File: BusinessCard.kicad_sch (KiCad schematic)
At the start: 4 parts, among them U1 NT3H2111W0FHKH

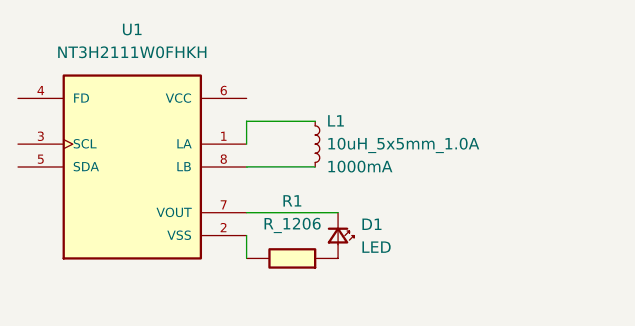
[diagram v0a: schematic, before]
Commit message: logos added to footprint
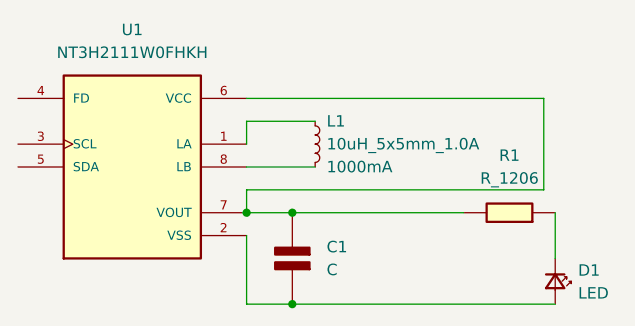
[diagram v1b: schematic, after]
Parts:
- added C1: C, PCM_4ms_Capacitor:CP_Elec_5x5.3, symbol PCM_Elektuur:C
- L1: footprint PCM_SparkFun-Coil:Inductor_4.7x4.7mm -> nfc:25X48MM_NFC_ANTENNA
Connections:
- net at U1.2 (VSS): now also D1.2 (A), C1.1 (+); no longer R1.1
- net at U1.6 (VCC): now also R1.1, U1.7 (VOUT), C1.2 (-)
- net at D1.1 (K): now also R1.2; no longer U1.7 (VOUT)
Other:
- moved on the sheet: D1, R1
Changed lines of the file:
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@@
 	(generator_version "9.0")
 	(paper "A4")
-	(wire
-		(pts
-			(xy 142.24 113.03) (xy 152.4 113.03)
+	(junction
+		(at 147.32 123.19)
+		(diameter 0)
+		(color 0 0 0 0)
+	)
+	(junction
+		(at 147.32 113.03)
+		(diameter 0)
+		(color 0 0 0 0)
+	)
+	(junction
+		(at 142.24 113.03)
+		(diameter 0)
+		(color 0 0 0 0)
+	)
+	(wire
+		(pts
+			(xy 147.32 123.19) (xy 142.24 123.19)
+		)
+		(stroke
+			(width 0)
+			(type default)
+		)
+	)
+	(wire
+		(pts
+			(xy 142.24 115.57) (xy 142.24 123.19)
+		)
+		(stroke
+			(width 0)
+			(type default)
+		)
+	)
+	(wire
+		(pts
+			(xy 142.24 100.33) (xy 175.26 100.33)
+		)
+		(stroke
+			(width 0)
+			(type default)
+		)
+	)
+	(wire
+		(pts
+			(xy 147.32 113.03) (xy 142.24 113.03)
+		)
+		(stroke
+			(width 0)
+			(type default)
+		)
+	)
+	(wire
+		(pts
+			(xy 175.26 100.33) (xy 175.26 110.49)
+		)
+		(stroke
+			(width 0)
+			(type default)
+		)
+	)
+	(wire
+		(pts
+			(xy 166.37 113.03) (xy 147.32 113.03)
+		)
+		(stroke
+			(width 0)
+			(type default)
+		)
+	)
+	(wire
+		(pts
+			(xy 176.53 118.11) (xy 176.53 113.03)
 		)
 		(stroke
@@
 	(wire
 		(pts
-			(xy 142.24 118.11) (xy 142.24 115.57)
+			(xy 142.24 110.49) (xy 142.24 113.03)
+		)
+		(stroke
+			(width 0)
+			(type default)
+		)
+	)
+	(wire
+		(pts
+			(xy 175.26 110.49) (xy 142.24 110.49)
 		)
 		(stroke
@@
 		(pts
 			(xy 149.86 102.87) (xy 142.24 102.87)
+		)
+		(stroke
+			(width 0)
+			(type default)
+		)
+	)
+	(wire
+		(pts
+			(xy 147.32 123.19) (xy 176.53 123.19)
 		)
 		(stroke
@@
 			)
 		)
-		(property "Footprint" "PCM_SparkFun-Coil:Inductor_4.7x4.7mm"
+		(property "Footprint" "nfc:25X48MM_NFC_ANTENNA"
 			(at 142.24 105.41 0)
 			(effects
@@
 				(path "/3ea08817-d3b1-4822-a9a3-fd820d6f9c9b"
 					(reference "L1")
+					(unit 1)
+				)
+			)
+		)
+	)
+	(symbol
+		(lib_id "PCM_Elektuur:C")
+		(at 147.32 118.11 180)
+		(unit 1)
+		(exclude_from_sim no)
+		(in_bom yes)
+		(on_board yes)
+		(dnp no)
+		(fields_autoplaced yes)
+		(property "Reference" "C1"
+			(at 151.13 116.8399 0)
+			(effects
+				(font
+					(size 1.27 1.27)
+				)
+				(justify right)
+			)
+		)
+		(property "Value" "C"
+			(at 151.13 119.3799 0)
+			(effects
+				(font
+					(size 1.27 1.27)
+				)
+				(justify right)
+			)
+		)
+		(property "Footprint" "PCM_4ms_Capacitor:CP_Elec_5x5.3"
+			(at 147.32 118.11 0)
+			(effects
+				(font
+					(size 1.27 1.27)
+				)
+				(hide yes)
+			)
+		)
+		(property "Datasheet" ""
+			(at 147.32 118.11 0)
+			(effects
+				(font
+					(size 1.27 1.27)
+				)
+				(hide yes)
+			)
+		)
+		(property "Description" "capacitor, non-polarized/bipolar"
+			(at 147.32 118.11 0)
+			(effects
+				(font
+					(size 1.27 1.27)
+				)
+				(hide yes)
+			)
+		)
+		(property "Indicator" "+"
+			(at 148.59 121.285 0)
+			(effects
+				(font
+					(size 1.27 1.27)
+				)
+				(hide yes)
+			)
+		)
+		(property "Rating" "V"
+			(at 147.955 114.935 0)
+			(effects
+				(font
+					(size 1.27 1.27)
+				)
+				(justify right)
+				(hide yes)
+			)
+		)
+		(pin "1"
+		)
+		(pin "2"
+		)
+		(instances
+			(project ""
+				(path "/3ea08817-d3b1-4822-a9a3-fd820d6f9c9b"
+					(reference "C1")
 					(unit 1)
 				)
@@
 	(symbol
 		(lib_id "PCM_fab:R_1206")
-		(at 147.32 118.11 90)
+		(at 171.45 113.03 90)
 		(unit 1)
 		(exclude_from_sim no)
@@
 		(fields_autoplaced yes)
 		(property "Reference" "R1"
-			(at 147.32 111.76 90)
+			(at 171.45 106.68 90)
 			(effects
 				(font
@@
 		)
 		(property "Value" "R_1206"
-			(at 147.32 114.3 90)
+			(at 171.45 109.22 90)
 			(effects
 				(font
@@
 		)
 		(property "Footprint" "PCM_fab:R_1206"
-			(at 147.32 118.11 90)
+			(at 171.45 113.03 90)
 			(effects
 				(font
@@
 		)
 		(property "Datasheet" "~"
-			(at 147.32 118.11 0)
+			(at 171.45 113.03 0)
 			(effects
 				(font
@@
 		)
 		(property "Description" "Resistor"
-			(at 147.32 118.11 0)
+			(at 171.45 113.03 0)
 			(effects
 				(font
@@
 	(symbol
 		(lib_id "PCM_SparkFun-LED:LED")
-		(at 152.4 115.57 270)
+		(at 176.53 120.65 270)
 		(unit 1)
 		(exclude_from_sim no)
@@
 		(fields_autoplaced yes)
 		(property "Reference" "D1"
-			(at 154.94 114.3634 90)
+			(at 179.07 119.4434 90)
 			(effects
 				(font
@@
 		)
 		(property "Value" "LED"
-			(at 154.94 116.9034 90)
+			(at 179.07 121.9834 90)
 			(effects
 				(font
@@
 		)
 		(property "Footprint" "PCM_SparkFun-LED:LED_0603_1608Metric"
-			(at 147.32 115.57 0)
+			(at 171.45 120.65 0)
 			(effects
 				(font
@@
 		)
 		(property "Datasheet" "~"
-			(at 144.78 115.57 0)
+			(at 168.91 120.65 0)
 			(effects
 				(font
@@
 		)
 		(property "Description" "Light emitting diode"
-			(at 139.7 115.57 0)
+			(at 163.83 120.65 0)
 			(effects
 				(font
@@
 		)
 		(property "PROD_ID" "LED-"
-			(at 142.24 115.57 0)
-			(effects
-				(font
+			(at 166.37 120.65 0)
+			(effects
+				(font

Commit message: Made a few design changes, started the intro
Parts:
- C1: footprint PCM_4ms_Capacitor:CP_Elec_5x5.3 -> nfc:CAPC1608X90N
- D1: footprint PCM_SparkFun-LED:LED_0603_1608Metric -> nfc:LED0805-R-RD
- R1: footprint PCM_fab:R_1206 -> nfc:C0603
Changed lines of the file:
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@@
 			)
 		)
-		(property "Footprint" "PCM_4ms_Capacitor:CP_Elec_5x5.3"
+		(property "Footprint" "nfc:CAPC1608X90N"
 			(at 147.32 118.11 0)
 			(effects
@@
 			)
 		)
-		(property "Footprint" "PCM_fab:R_1206"
+		(property "Footprint" "nfc:C0603"
 			(at 171.45 113.03 90)
 			(effects
@@
 			)
 		)
-		(property "Footprint" "PCM_SparkFun-LED:LED_0603_1608Metric"
+		(property "Footprint" "nfc:LED0805-R-RD"
 			(at 171.45 120.65 0)
 			(effects
